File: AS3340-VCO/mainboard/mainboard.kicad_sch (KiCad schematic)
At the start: 80 parts, among them J1 Conn_02x05_Odd_Even, J2 Conn_01x03, J3 Conn_02x05_Odd_Even, Q1 Q_NPN_EBC, Q2 Q_NPN_EBC, U1 TL071, U2 TL074, U3 AS3340, U4 TL074

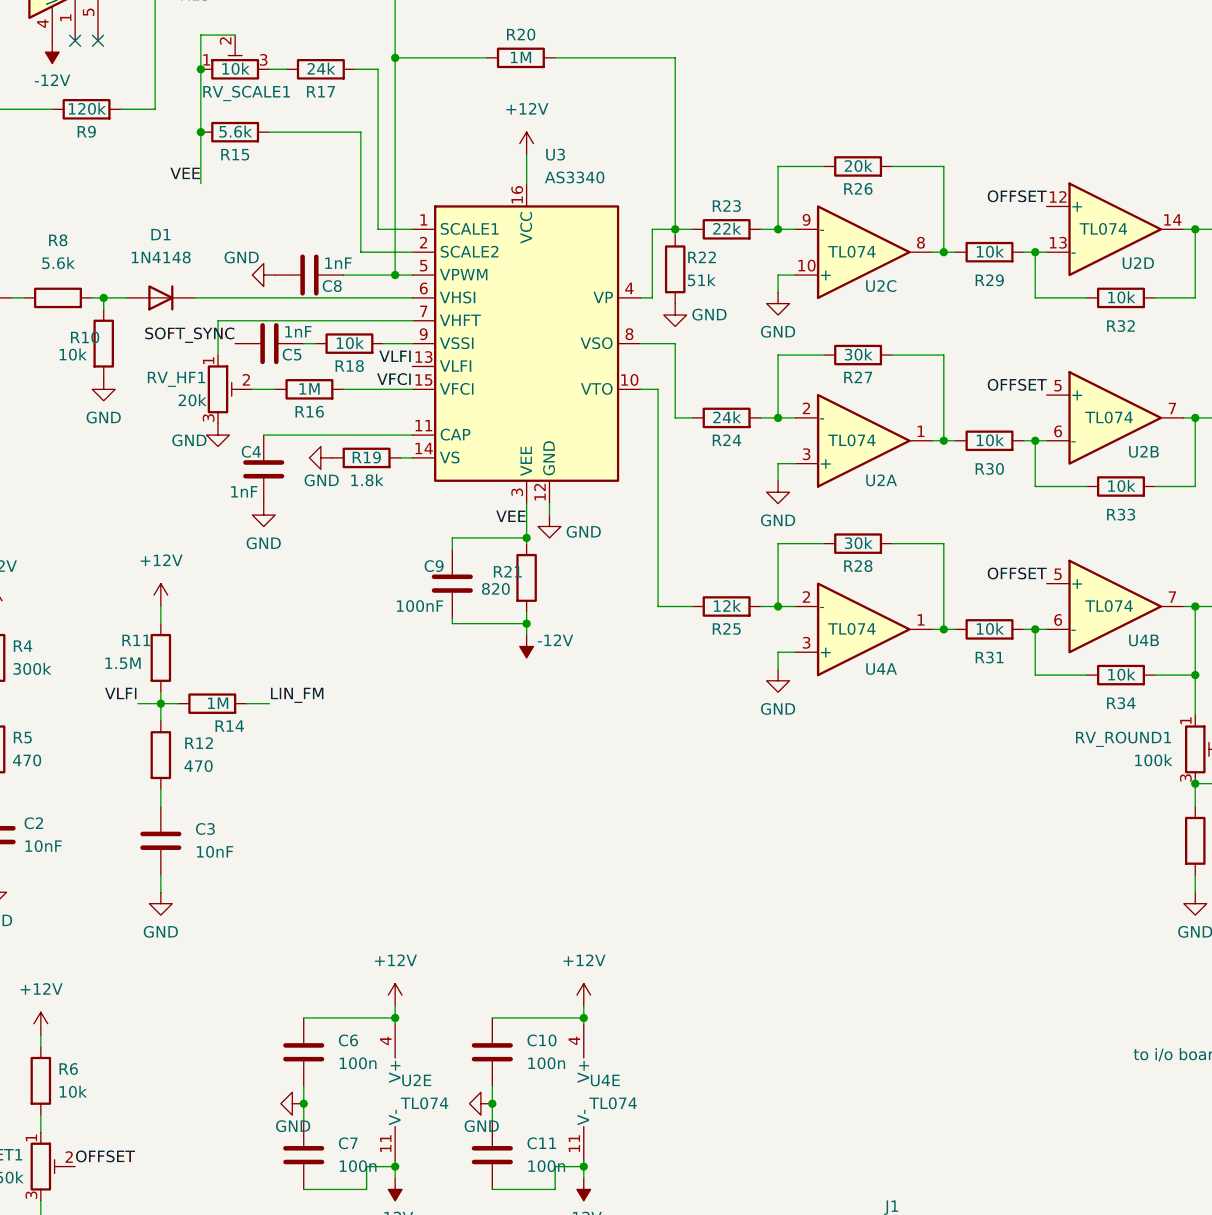
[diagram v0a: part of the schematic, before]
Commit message: Add -5V regulator so internal zener doesn't heat up
The internal zener of the AS3340 chip will heat up the chip, causing it
to take ~45 minutes to create a stable frequency. With an external -5V
it only takes 15 minutes.
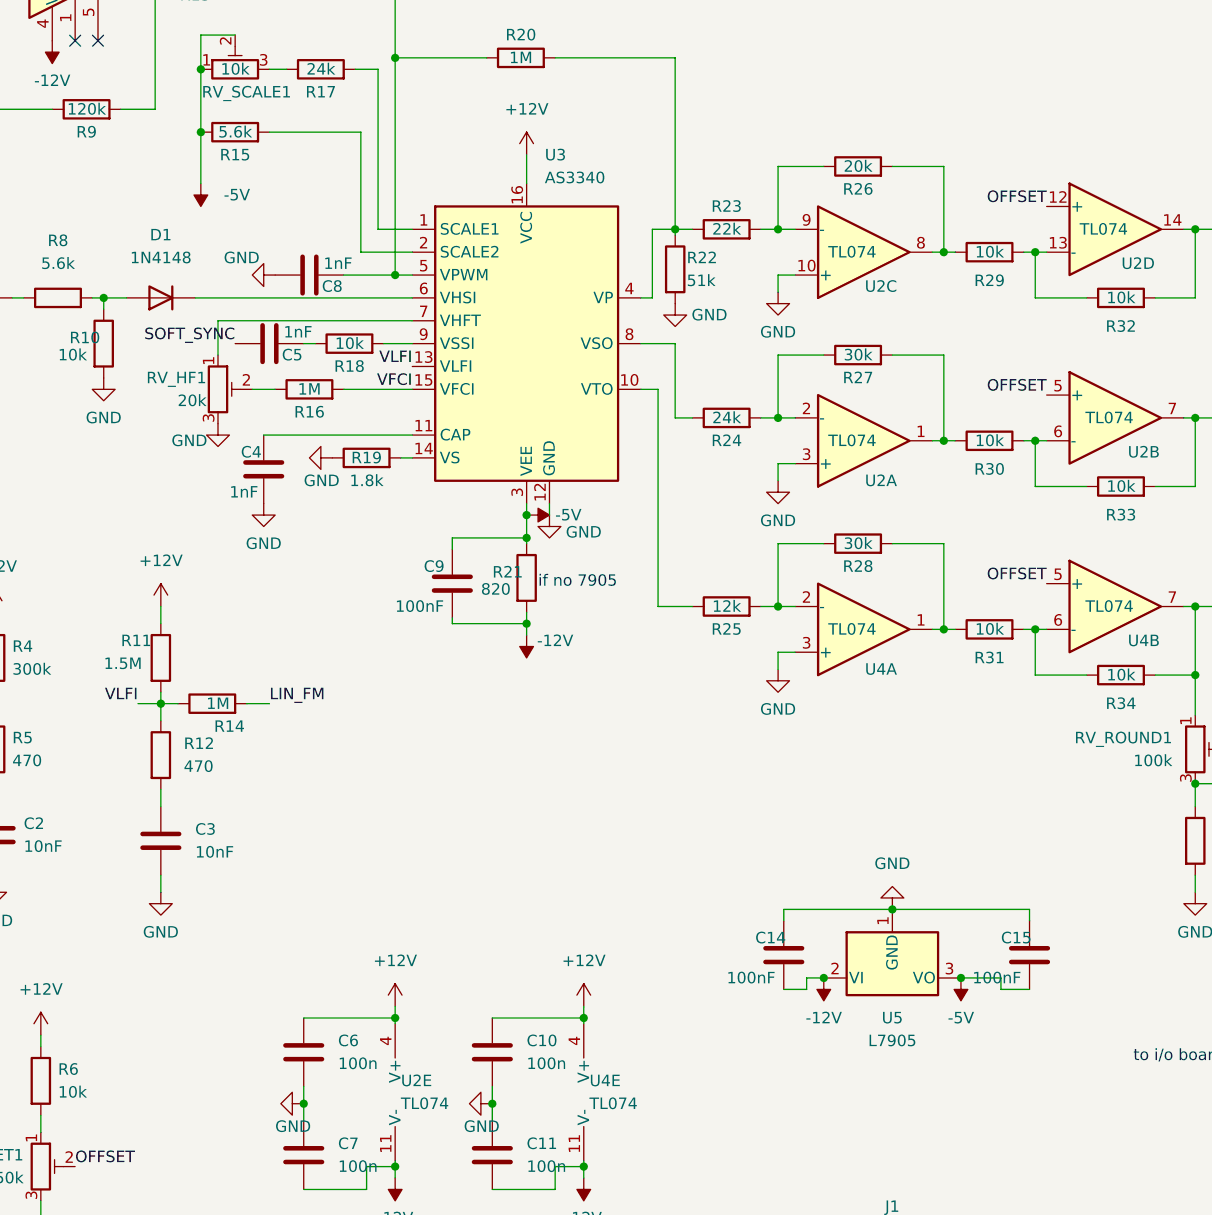
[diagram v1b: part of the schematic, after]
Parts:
- added C14, C15: 100nF, Capacitor_SMD:C_0603_1608Metric_Pad1.08x0.95mm_HandSolder, symbol Device:C
- added U5: L7905, Package_TO_SOT_SMD:SOT-89-3_Handsoldering, symbol Regulator_Linear:L7905
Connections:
- net -12V: now also C14.2, U5.2 (VI)
- net GND: now also C14.1, C15.1, U5.1 (GND)
- net VEE renamed -5V
- net -5V: now also C15.2, U5.3 (VO)
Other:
- note added: "if no 7905"

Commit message: Finish DuinoRack hardware, final touches on AS3340 VCO
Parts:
- removed U5: L7905, Package_TO_SOT_SMD:SOT-89-3_Handsoldering, symbol Regulator_Linear:L7905
- added C16: 560p, Capacitor_SMD:C_0603_1608Metric_Pad1.08x0.95mm_HandSolder, symbol Device:C
- added C17, C18: 100nF, Capacitor_SMD:C_0603_1608Metric_Pad1.08x0.95mm_HandSolder, symbol Device:C
- added H1: MountingHole, Library:MountingHole_3.2mm_M3_NoCourt, symbol Mechanical:MountingHole
- added J4: TP1, Connector_PinHeader_2.54mm:PinHeader_1x01_P2.54mm_Vertical, symbol Connector:Conn_01x01_Male
- added J5: TP2, Connector_PinHeader_2.54mm:PinHeader_1x01_P2.54mm_Vertical, symbol Connector:Conn_01x01_Male
- added JP1: SET_REF_PITCH, Connector_PinHeader_2.54mm:PinHeader_1x02_P2.54mm_Vertical, symbol Jumper:Jumper_2_Open
- added R51: 1k6, Resistor_SMD:R_0603_1608Metric_Pad0.98x0.95mm_HandSolder, symbol Device:R
- added R52, R55: 1k, Resistor_SMD:R_0603_1608Metric_Pad0.98x0.95mm_HandSolder, symbol Device:R
- added R53, R54, R56, R57: 100k, Resistor_SMD:R_0603_1608Metric_Pad0.98x0.95mm_HandSolder, symbol Device:R
- added R58: 470k, Resistor_SMD:R_0603_1608Metric_Pad0.98x0.95mm_HandSolder, symbol Device:R
- added REFIND_C6, TRIM_7V1: 100k, Potentiometer_THT:Potentiometer_Bourns_3266Y_Vertical, symbol Device:R_Potentiometer_Trim
- added REF_PITCH_C6: 10k, Potentiometer_THT:Potentiometer_Bourns_3266Y_Vertical, symbol Device:R_Potentiometer_Trim
- added SCALE_ADJ1: 500, Potentiometer_THT:Potentiometer_Bourns_3266Y_Vertical, symbol Device:R_Potentiometer_Trim
- added TP1: 7V, Connector_PinHeader_2.54mm:PinHeader_1x01_P2.54mm_Vertical, symbol Connector:TestPoint
- added TP2: 1V, Connector_PinHeader_2.54mm:PinHeader_1x01_P2.54mm_Vertical, symbol Connector:TestPoint
- added TRIM_1V1: 200k, Potentiometer_THT:Potentiometer_Bourns_3266Y_Vertical, symbol Device:R_Potentiometer_Trim
- added U5, U6: TL431DBZ, Package_TO_SOT_SMD:SOT-23, symbol Reference_Voltage:TL431DBZ
- J1: value Conn_02x05_Odd_Even -> Conn_02x06_Odd_Even; footprint Connector_PinHeader_2.54mm:PinHeader_2x05_P2.54mm_Vertical -> Connector_PinHeader_2.54mm:PinHeader_2x06_P2.54mm_Vertical; symbol Connector_Generic:Conn_02x05_Odd_Even -> Connector_Generic:Conn_02x06_Odd_Even
- J2: value Conn_01x03 -> Conn_01x04; footprint Connector_PinHeader_2.54mm:PinHeader_1x03_P2.54mm_Vertical -> Connector_PinHeader_2.54mm:PinHeader_1x04_P2.54mm_Vertical; symbol Connector_Generic:Conn_01x03 -> Connector_Generic:Conn_01x04
- R11: value 1.5M -> 1.3M *
- R17: value 24k -> 18k
- R19: value 1.8k -> 22k
- R21: value 820 -> 5.6k
- R4: value 300k -> 220k
- TEMPCO_ADJ1: renamed from RV_SCALE1; value 10k -> 5k
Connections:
- net +12V: now also R55.1, REFIND_C6.1, REF_PITCH_C6.1; no longer R11.1, R4.1
- net -12V: now also R52.1; no longer C14.2, C9.2, R21.2
- net -5V: now also C14.2, R52.2, R54.2, U5.3 (A); no longer TEMPCO_ADJ1.1, TEMPCO_ADJ1.2
- net GND: now also C4.2, C9.2, R19.2, C16.2, C17.2, C18.2, JP1.1 (A), R53.1, R57.2, SCALE_ADJ1.2, SCALE_ADJ1.3, U5.1 (K), U6.3 (A); no longer C4.1, R19.1
- net CAP: now reaches U3.11 (CAP)
- net CAP: now also C4.1, J1.12 (Pin_12); no longer C4.2
- net at R15.2, U3.2 (SCALE2): now also J5.1 (Pin_1)
- net at U3.14 (VS): now also C16.1, JP1.2 (B), R51.1; no longer R19.2
- new net: R53.2, R54.1, U5.2 (REF)
- new net: R51.2, SCALE_ADJ1.1
- new net: J4.1 (Pin_1), R21.2, TEMPCO_ADJ1.1, TEMPCO_ADJ1.2
- new net: R19.1, REF_PITCH_C6.3
- new net: R11.1, REF_PITCH_C6.2
- new net: R58.1, TRIM_1V1.3
- new net: R56.2, R57.1, U6.2 (REF)
- new net: R4.1, REFIND_C6.2, REFIND_C6.3
- new net: R56.1, TRIM_7V1.3
- new net +1.000V: J1.11 (Pin_11), R58.2, TP2.1
- new net +7.000V: C17.1, C18.1, J2.4 (Pin_4), R55.2, TP1.1, TRIM_1V1.1, TRIM_1V1.2, TRIM_7V1.1, TRIM_7V1.2, U6.1 (K)
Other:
- note removed: "if no 7905"
- moved on the sheet: C2, C4, C9, R17, R4, R5, TEMPCO_ADJ1

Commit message: Saving latest changes
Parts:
- added TP3: GND, Connector_PinHeader_2.54mm:PinHeader_1x01_P2.54mm_Vertical, symbol Connector:TestPoint
- J4: value TP1 -> TEMP1
- J5: value TP2 -> TEMP2
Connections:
- net GND: now also TP3.1
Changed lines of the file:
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@@
   (junction (at 179.07 125.095) (diameter 0) (color 0 0 0 0)
   )
+  (junction (at 256.54 152.4) (diameter 0) (color 0 0 0 0)
+  )
   (junction (at 257.81 41.275) (diameter 0) (color 0 0 0 0)
   )
@@
     (stroke (width 0) (type default) (color 0 0 0 0))
   )
-  (wire (pts (xy 250.19 152.4) (xy 259.715 152.4))
+  (wire (pts (xy 250.19 152.4) (xy 256.54 152.4))
     (stroke (width 0) (type default) (color 0 0 0 0))
   )
@@
     (stroke (width 0) (type default) (color 0 0 0 0))
   )
+  (wire (pts (xy 256.54 152.4) (xy 259.715 152.4))
+    (stroke (width 0) (type default) (color 0 0 0 0))
+  )
   (wire (pts (xy 57.15 26.67) (xy 74.93 26.67))
     (stroke (width 0) (type default) (color 0 0 0 0))
@@
       (effects (font (size 1.27 1.27)) (justify right))
     )
-    (property "Value" "TP2" (id 1) (at 63.5 50.1649 90)
+    (property "Value" "TEMP2" (id 1) (at 63.5 50.1649 90)
       (effects (font (size 1.27 1.27)) (justify right))
     )
@@
     (pin "4")
   )
+  (symbol (lib_id "Connector:TestPoint") (at 256.54 152.4 180) (unit 1)
+    (in_bom yes) (on_board yes) (fields_autoplaced)
+    (property "Reference" "TP3" (id 0) (at 259.08 154.4319 0)
+      (effects (font (size 1.27 1.27)) (justify right))
+    )
+    (property "Value" "GND" (id 1) (at 259.08 156.9719 0)
+      (effects (font (size 1.27 1.27)) (justify right))
+    )
+    (property "Footprint" "Connector_PinHeader_2.54mm:PinHeader_1x01_P2.54mm_Vertical" (id 2) (at 251.46 152.4 0)
+      (effects (font (size 1.27 1.27)) hide)
+    )
+    (property "Datasheet" "~" (id 3) (at 251.46 152.4 0)
+      (effects (font (size 1.27 1.27)) hide)
+    )
+    (pin "1")
+  )
   (symbol (lib_id "Device:R") (at 241.935 108.585 90) (unit 1)
     (in_bom yes) (on_board yes)
@@
       (effects (font (size 1.27 1.27)) (justify right))
     )
-    (property "Value" "TP1" (id 1) (at 59.69 30.4799 90)
+    (property "Value" "TEMP1" (id 1) (at 59.69 30.4799 90)
       (effects (font (size 1.27 1.27)) (justify right))
     )
@@
     )
     (path "/ba304b59-ca26-4560-ab68-189a5793ef7a"
-      (reference "J4") (unit 1) (value "TP1") (footprint "Connector_PinHeader_2.54mm:PinHeader_1x01_P2.54mm_Vertical")
+      (reference "J4") (unit 1) (value "TEMP1") (footprint "Connector_PinHeader_2.54mm:PinHeader_1x01_P2.54mm_Vertical")
     )
     (path "/56470b97-c882-44f1-ac13-fca0d111fee4"
-      (reference "J5") (unit 1) (value "TP2") (footprint "Connector_PinHeader_2.54mm:PinHeader_1x01_P2.54mm_Vertical")
+      (reference "J5") (unit 1) (value "TEMP2") (footprint "Connector_PinHeader_2.54mm:PinHeader_1x01_P2.54mm_Vertical")
     )
     (path "/0904c923-f31f-424a-8802-26f227300928"
@@
       (reference "TP2") (unit 1) (value "1V") (footprint "Connector_PinHeader_2.54mm:PinHeader_1x01_P2.54mm_Vertical")
     )
+    (path "/b89270b9-dd95-4086-a42a-0add0bb8fdff"
+      (reference "TP3") (unit 1) (value "GND") (footprint "Connector_PinHeader_2.54mm:PinHeader_1x01_P2.54mm_Vertical")
+    )
     (path "/db76ce59-fed5-4d3b-912b-6d6688bc73b3"

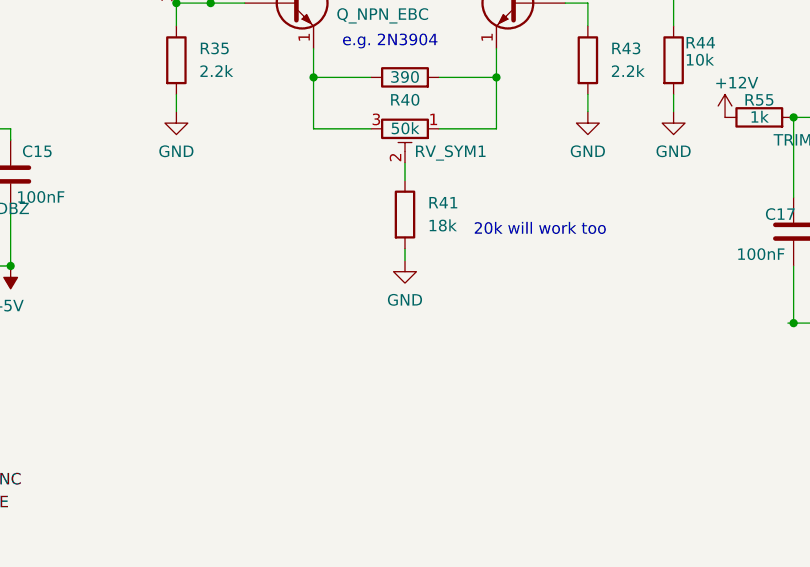
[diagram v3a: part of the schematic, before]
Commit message: Apply rev1 fixes to AS3340 VCO
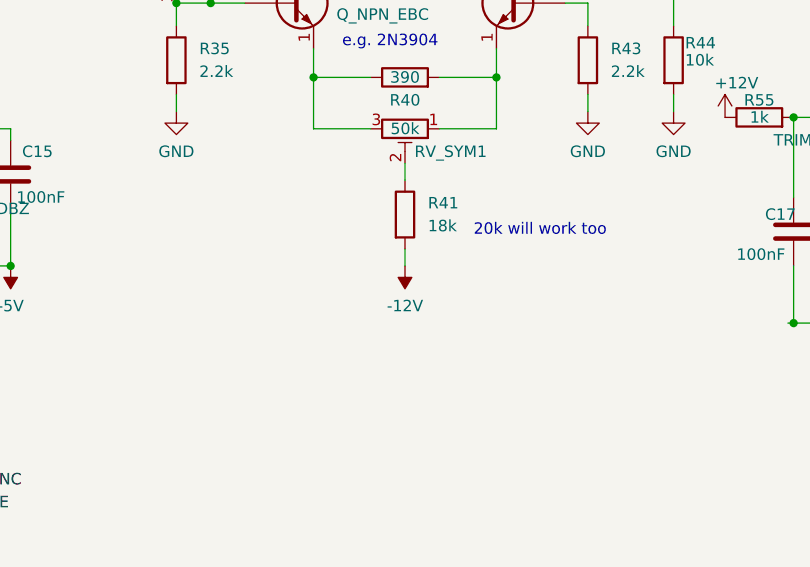
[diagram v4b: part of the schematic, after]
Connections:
- net -12V: now also R41.2
- net GND: no longer R41.2
